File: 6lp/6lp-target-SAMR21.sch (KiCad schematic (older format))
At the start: 23 parts, among them SW401 SW_PUSH, T401 2450BM15A0015, U401 SAMR21E, X401 CRYSTAL-4

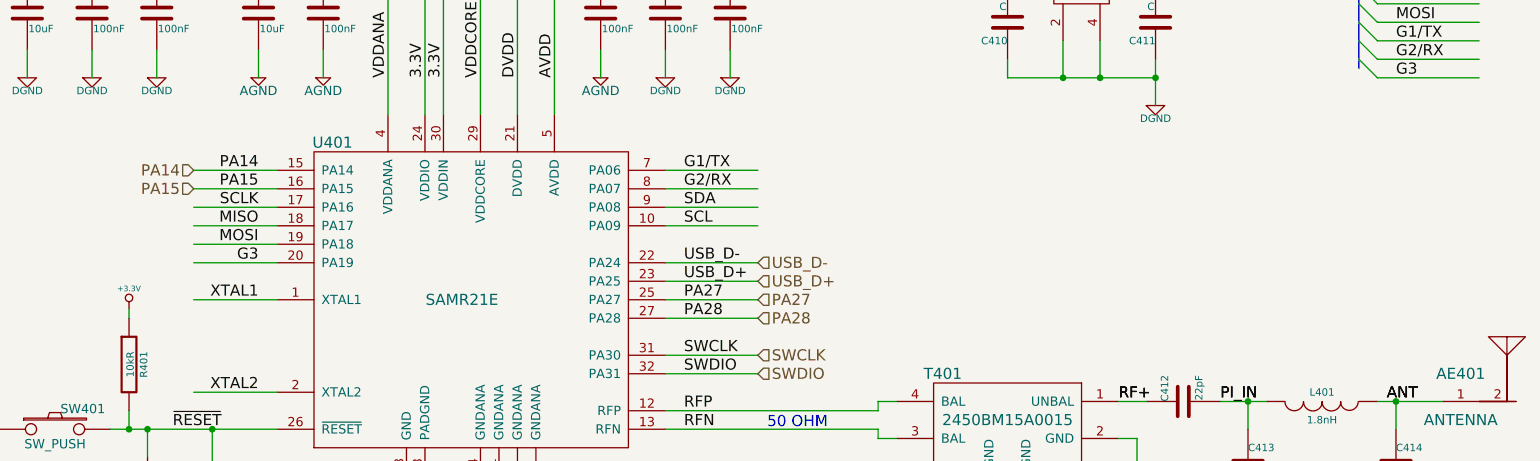
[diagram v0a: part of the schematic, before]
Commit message: proper pix muxing
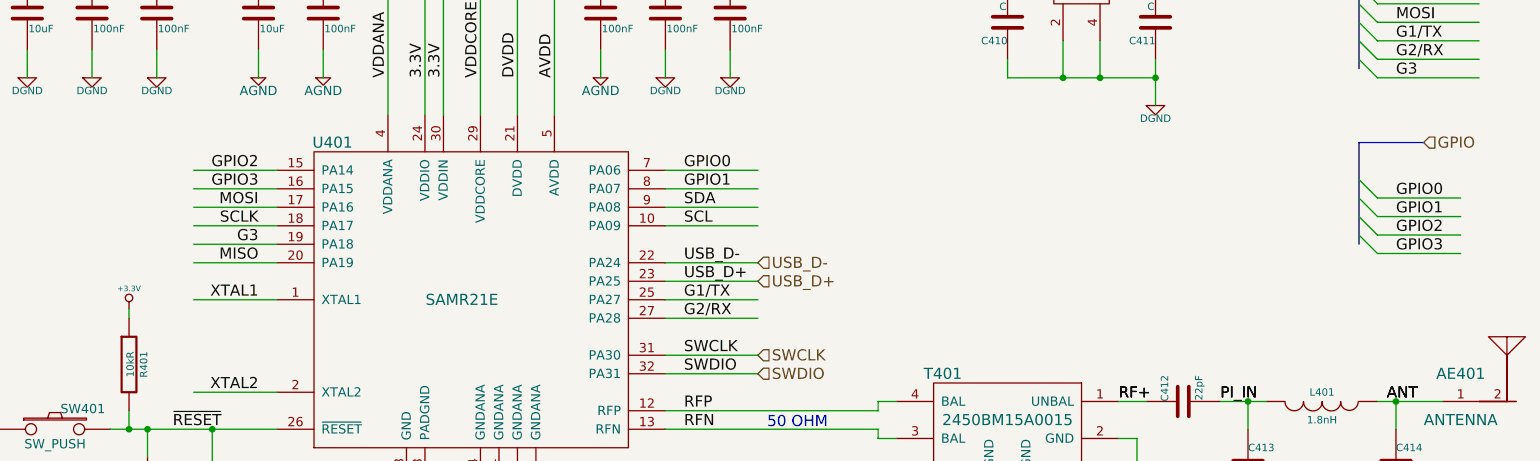
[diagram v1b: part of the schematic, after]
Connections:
- net labels added: GPIO, GPIO0, GPIO1, GPIO2, GPIO3
- net labels removed: PA14, PA15, PA27, PA28
- wire segments 111 -> 115
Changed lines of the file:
@@
 Text Label 5450 4650 0    60   ~ 0
 SWDIO
-Text Label 5450 4250 0    60   ~ 0
-PA27
-Text Label 5450 4350 0    60   ~ 0
-PA28
 $Comp
 L BALUN-6 T401
@@
 Text Label 5450 4150 0    60   ~ 0
 USB_D+
+Text Label 3150 3850 2    60   ~ 0
+SCLK
+Text Label 3150 4050 2    60   ~ 0
+MISO
 Text Label 3150 3750 2    60   ~ 0
-SCLK
-Text Label 3150 3850 2    60   ~ 0
-MISO
-Text Label 3150 3950 2    60   ~ 0
 MOSI
 Text Label 3150 4250 2    60   ~ 0
@@
 Text Label 3150 4750 2    60   ~ 0
 XTAL2
-Text Label 3150 4050 2    60   ~ 0
+Text Label 3150 3950 2    60   ~ 0
 G3
-Text Label 5450 3550 0    60   ~ 0
+Text Label 5450 4250 0    60   ~ 0
 G1/TX
-Text Label 5450 3650 0    60   ~ 0
+Text Label 5450 4350 0    60   ~ 0
 G2/RX
 Text Label 5450 3750 0    60   ~ 0
@@
 Text Label 5450 3850 0    60   ~ 0
 SCL
-Text Label 3150 3550 2    60   ~ 0
-PA14
-Text Label 3150 3650 2    60   ~ 0
-PA15
 $Comp
 L SW_PUSH SW401
@@
 Text HLabel 5850 4150 2    60   Input ~ 0
 USB_D+
-Text HLabel 5850 4250 2    60   Input ~ 0
-PA27
-Text HLabel 5850 4350 2    60   Input ~ 0
-PA28
 Text HLabel 5850 4550 2    60   Input ~ 0
 SWCLK
@@
 Text Label 9300 2550 0    60   ~ 0
 SCLK
-Text HLabel 2800 3550 0    60   Input ~ 0
-PA14
-Text HLabel 2800 3650 0    60   Input ~ 0
-PA15
+Text HLabel 9450 3400 2    60   Input ~ 0
+GPIO
+Wire Bus Line
+	9450 3400 9100 3400
+Entry Wire Line
+	9100 3600 9200 3700
+Entry Wire Line
+	9100 3700 9200 3800
+Entry Wire Line
+	9100 3800 9200 3900
+Entry Wire Line
+	9100 3900 9200 4000
+Wire Wire Line
+	9200 3700 9650 3700
+Wire Wire Line
+	9200 3800 9650 3800
+Wire Wire Line
+	9200 3900 9650 3900
+Wire Wire Line
+	9200 4000 9650 4000
+Wire Bus Line
+	9100 3400 9100 3950
+Text Label 9300 3700 0    60   ~ 0
+GPIO0
+Text Label 9300 3800 0    60   ~ 0
+GPIO1
+Text Label 9300 3900 0    60   ~ 0
+GPIO2
+Text Label 9300 4000 0    60   ~ 0
+GPIO3
+Text Label 5450 3550 0    60   ~ 0
+GPIO0
+Text Label 5450 3650 0    60   ~ 0
+GPIO1
+Text Label 3150 3550 2    60   ~ 0
+GPIO2
+Text Label 3150 3650 2    60   ~ 0
+GPIO3
 $EndSCHEMATC

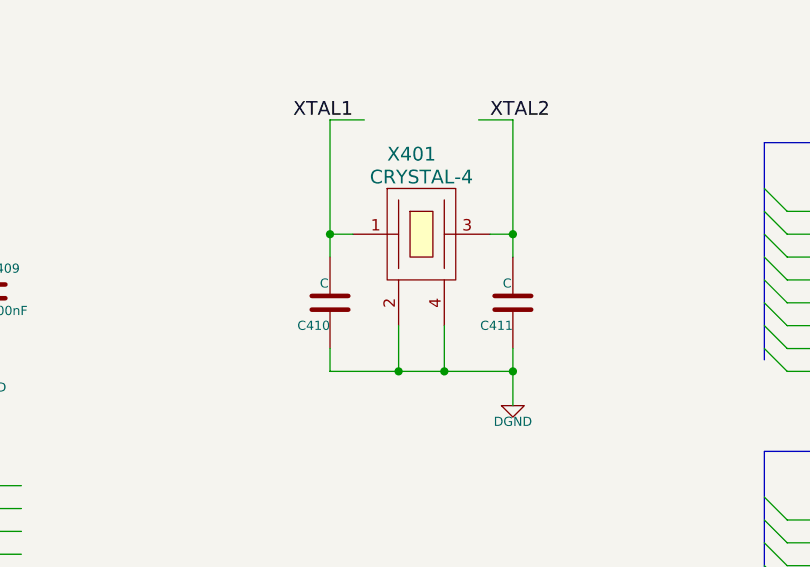
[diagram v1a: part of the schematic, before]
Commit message: redid annotation so the refdes aren't HUGE
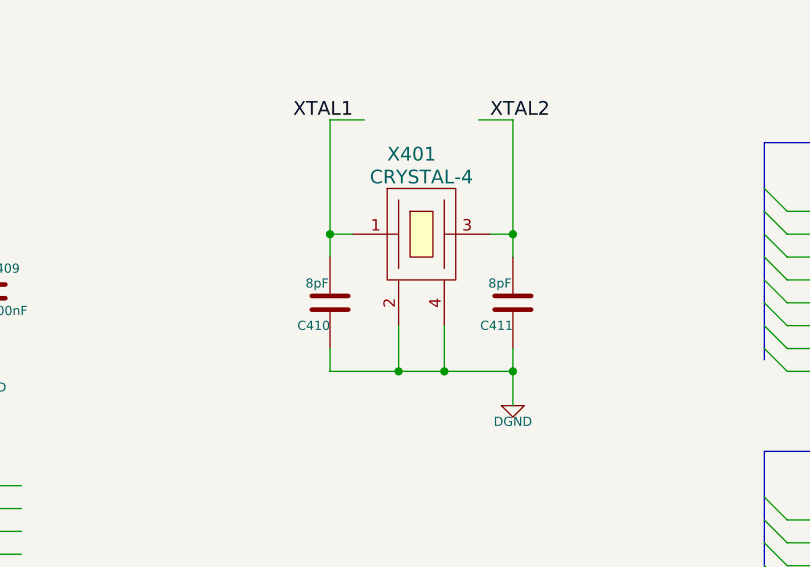
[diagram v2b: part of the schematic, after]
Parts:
- C410, C411: value C -> 8pF
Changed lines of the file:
@@
 P 8000 2750
 F 0 "C411" H 8000 2850 40  0000 L CNN
-F 1 "C" H 8006 2665 40  0000 L CNN
+F 1 "8pF" H 8006 2665 40  0000 L CNN
 F 2 "Capacitors_SMD:C_0402" H 8038 2600 30  0001 C CNN
 F 3 "" H 8000 2750 60  0000 C CNN
@@
 P 7200 2750
 F 0 "C410" H 7200 2850 40  0000 L CNN
-F 1 "C" H 7206 2665 40  0000 L CNN
+F 1 "8pF" H 7206 2665 40  0000 L CNN
 F 2 "Capacitors_SMD:C_0402" H 7238 2600 30  0001 C CNN
 F 3 "" H 7200 2750 60  0000 C CNN

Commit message: component file is ready...i hope
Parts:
- renumbered AE401 to AE1, C406 to C10, C407 to C11, C408 to C12, C409 to C13, C410 to C14, C411 to C15, C412 to C16, C413 to C17, C414 to C18, C401 to C5, C402 to C6, C403 to C7, C404 to C8, C405 to C9, FB401 to FB1, JP401 to JP1, L401 to L2, R401 to R10, SW401 to SW1, T401 to T1, U401 to U3, X401 to X1

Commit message: i has a board! it has a lot of parts!
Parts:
- C10, C11, C12, C13, C14, C15, C16, C17, C18, C6, C7, C8, L2: footprint Capacitors_SMD:C_0402 -> parts:SMD-0402
- C5: footprint Capacitors_SMD:C_0402 -> SMD_Packages:SMD-0805
- C9: footprint Capacitors_SMD:C_0805 -> SMD_Packages:SMD-0805
- FB1: footprint Capacitors_SMD:C_0603 -> parts:SMD-0402
- JP1: footprint (none) -> SMD_Packages:SMD-0201_r
- R10: footprint Resistors_SMD:R_0402 -> parts:SMD-0402
- SW1: footprint (none) -> Pin_Headers:Pin_Header_Straight_1x02
- X1: footprint (none) -> parts:TSX-3225
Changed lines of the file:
@@
 EESchema Schematic File Version 2
 LIBS:power
-LIBS:device
-LIBS:transistors
-LIBS:conn
-LIBS:linear
-LIBS:regul
-LIBS:74xx
-LIBS:cmos4000
-LIBS:adc-dac
-LIBS:memory
-LIBS:xilinx
-LIBS:special
-LIBS:microcontrollers
-LIBS:dsp
-LIBS:microchip
-LIBS:analog_switches
-LIBS:motorola
-LIBS:texas
-LIBS:intel
-LIBS:audio
-LIBS:interface
-LIBS:digital-audio
-LIBS:philips
-LIBS:display
-LIBS:cypress
-LIBS:siliconi
-LIBS:opto
-LIBS:atmel
-LIBS:contrib
-LIBS:valves
-LIBS:parts
 LIBS:6lp-cache
 EELAYER 24 0
@@
 F 0 "C13" H 5700 2800 40  0000 L CNN
 F 1 "100nF" H 5706 2615 40  0000 L CNN
-F 2 "Capacitors_SMD:C_0402" H 5738 2550 30  0001 C CNN
+F 2 "parts:SMD-0402" H 5738 2550 30  0001 C CNN
 F 3 "" H 5700 2700 60  0000 C CNN
 	1    5700 2700
@@
 F 0 "C10" H 3500 2800 40  0000 L CNN
 F 1 "100nF" H 3506 2615 40  0000 L CNN
-F 2 "Capacitors_SMD:C_0402" H 3538 2550 30  0001 C CNN
+F 2 "parts:SMD-0402" H 3538 2550 30  0001 C CNN
 F 3 "" H 3500 2700 60  0000 C CNN
 	1    3500 2700
@@
 F 0 "C6" H 2250 2800 40  0000 L CNN
 F 1 "100nF" H 2256 2615 40  0000 L CNN
-F 2 "Capacitors_SMD:C_0402" H 2288 2550 30  0001 C CNN
+F 2 "parts:SMD-0402" H 2288 2550 30  0001 C CNN
 F 3 "" H 2250 2700 60  0000 C CNN
 	1    2250 2700
@@
 F 0 "C8" H 2600 2800 40  0000 L CNN
 F 1 "100nF" H 2606 2615 40  0000 L CNN
-F 2 "Capacitors_SMD:C_0402" H 2638 2550 30  0001 C CNN
+F 2 "parts:SMD-0402" H 2638 2550 30  0001 C CNN
 F 3 "" H 2600 2700 60  0000 C CNN
 	1    2600 2700
@@
 F 0 "C11" H 5000 2800 40  0000 L CNN
 F 1 "100nF" H 5006 2615 40  0000 L CNN
-F 2 "Capacitors_SMD:C_0402" H 5038 2550 30  0001 C CNN
+F 2 "parts:SMD-0402" H 5038 2550 30  0001 C CNN
 F 3 "" H 5000 2700 60  0000 C CNN
 	1    5000 2700
@@
 F 0 "C12" H 5350 2800 40  0000 L CNN
 F 1 "100nF" H 5356 2615 40  0000 L CNN
-F 2 "Capacitors_SMD:C_0402" H 5388 2550 30  0001 C CNN
+F 2 "parts:SMD-0402" H 5388 2550 30  0001 C CNN
 F 3 "" H 5350 2700 60  0000 C CNN
 	1    5350 2700
@@
 F 0 "FB1" H 2700 2100 60  0000 C CNN
 F 1 "10uH" H 2700 1850 60  0000 C CNN
-F 2 "Capacitors_SMD:C_0603" H 2700 1950 60  0001 C CNN
+F 2 "parts:SMD-0402" H 2700 1950 60  0001 C CNN
 F 3 "" H 2700 1950 60  0000 C CNN
 	1    2700 1950
@@
 F 0 "C9" H 3150 2800 40  0000 L CNN
 F 1 "10uF" H 3156 2615 40  0000 L CNN
-F 2 "Capacitors_SMD:C_0805" H 3188 2550 30  0001 C CNN
+F 2 "SMD_Packages:SMD-0805" H 3188 2550 30  0001 C CNN
 F 3 "" H 3150 2700 60  0000 C CNN
 	1    3150 2700
@@
 F 0 "C5" H 1900 2800 40  0000 L CNN
 F 1 "10uF" H 1906 2615 40  0000 L CNN
-F 2 "Capacitors_SMD:C_0402" H 1938 2550 30  0001 C CNN
+F 2 "SMD_Packages:SMD-0805" H 1938 2550 30  0001 C CNN
 F 3 "" H 1900 2700 60  0000 C CNN
 	1    1900 2700
@@
 F 0 "C7" H 2550 5400 40  0000 L CNN
 F 1 "100nF" H 2556 5215 40  0000 L CNN
-F 2 "Capacitors_SMD:C_0402" H 2588 5150 30  0001 C CNN
+F 2 "parts:SMD-0402" H 2588 5150 30  0001 C CNN
 F 3 "" H 2550 5300 60  0000 C CNN
 	1    2550 5300
@@
 F 0 "R10" V 2530 4600 40  0000 C CNN
 F 1 "10kR" V 2457 4601 40  0000 C CNN
-F 2 "Resistors_SMD:R_0402" V 2380 4600 30  0001 C CNN
+F 2 "parts:SMD-0402" V 2380 4600 30  0001 C CNN
 F 3 "" H 2450 4600 30  0000 C CNN
 	1    2450 4600
@@
 F 0 "C16" H 8150 4900 40  0000 L CNN
 F 1 "22pF" H 8156 4715 40  0000 L CNN
-F 2 "Capacitors_SMD:C_0402" H 8188 4650 30  0001 C CNN
+F 2 "parts:SMD-0402" H 8188 4650 30  0001 C CNN
 F 3 "" H 8150 4800 60  0000 C CNN
 	1    8150 4800
@@
 F 0 "C17" H 8500 5250 40  0000 L CNN
 F 1 "1.2pF" H 8506 5065 40  0000 L CNN
-F 2 "Capacitors_SMD:C_0402" H 8538 5000 30  0001 C CNN
+F 2 "parts:SMD-0402" H 8538 5000 30  0001 C CNN
 F 3 "" H 8500 5150 60  0000 C CNN
 	1    8500 5150
@@
 F 0 "L2" V 8850 4800 40  0000 C CNN
 F 1 "1.8nH" V 9000 4800 40  0000 C CNN
-F 2 "Capacitors_SMD:C_0402" H 8900 4800 60  0001 C CNN
+F 2 "parts:SMD-0402" H 8900 4800 60  0001 C CNN
 F 3 "" H 8900 4800 60  0000 C CNN
 	1    8900 4800
@@
 F 0 "C18" H 9300 5250 40  0000 L CNN
 F 1 "DNP" H 9306 5065 40  0000 L CNN
-F 2 "Capacitors_SMD:C_0402" H 9338 5000 30  0001 C CNN
+F 2 "parts:SMD-0402" H 9338 5000 30  0001 C CNN
 F 3 "" H 9300 5150 60  0000 C CNN
 	1    9300 5150
@@
 F 0 "SW1" H 2200 5060 50  0000 C CNN
 F 1 "SW_PUSH" H 2050 4870 50  0000 C CNN
-F 2 "" H 2050 4950 60  0000 C CNN
+F 2 "Pin_Headers:Pin_Header_Straight_1x02" H 2050 4950 60  0001 C CNN
 F 3 "" H 2050 4950 60  0000 C CNN
 	1    2050 4950
@@
 F 0 "C15" H 8000 2850 40  0000 L CNN
 F 1 "8pF" H 8006 2665 40  0000 L CNN
-F 2 "Capacitors_SMD:C_0402" H 8038 2600 30  0001 C CNN
+F 2 "parts:SMD-0402" H 8038 2600 30  0001 C CNN
 F 3 "" H 8000 2750 60  0000 C CNN
 	1    8000 2750
@@
 F 0 "C14" H 7200 2850 40  0000 L CNN
 F 1 "8pF" H 7206 2665 40  0000 L CNN
-F 2 "Capacitors_SMD:C_0402" H 7238 2600 30  0001 C CNN
+F 2 "parts:SMD-0402" H 7238 2600 30  0001 C CNN
 F 3 "" H 7200 2750 60  0000 C CNN
 	1    7200 2750
@@
 F 0 "X1" H 7450 2800 60  0000 L CNN
 F 1 "CRYSTAL-4" H 7600 2700 60  0000 C CNN
-F 2 "" H 7600 2450 60  0000 C CNN
+F 2 "parts:TSX-3225" H 7600 2450 60  0001 C CNN
 F 3 "" H 7600 2450 60  0000 C CNN
 	1    7600 2450
@@
 F 0 "JP1" H 3650 7300 60  0000 C CNN
 F 1 "JUMPER" H 3650 7070 40  0000 C CNN
-F 2 "" H 3650 7150 60  0000 C CNN
+F 2 "SMD_Packages:SMD-0201_r" H 3650 7150 60  0001 C CNN
 F 3 "" H 3650 7150 60  0000 C CNN
 	1    3650 7150

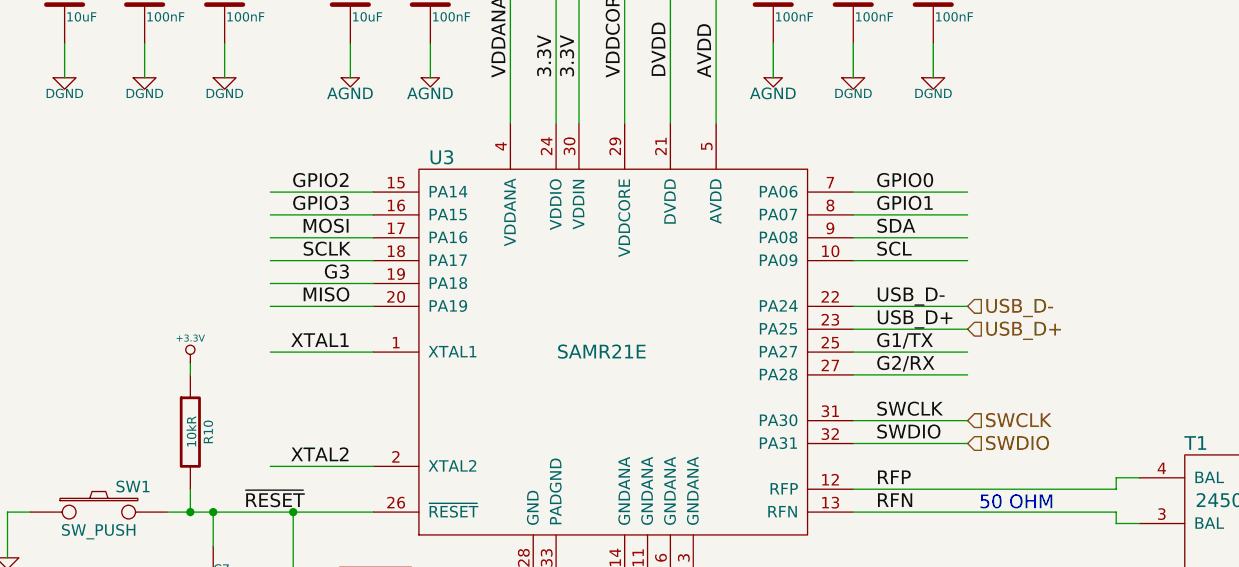
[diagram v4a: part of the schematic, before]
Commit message: pcb work...also labels did not work how i thought they did :/
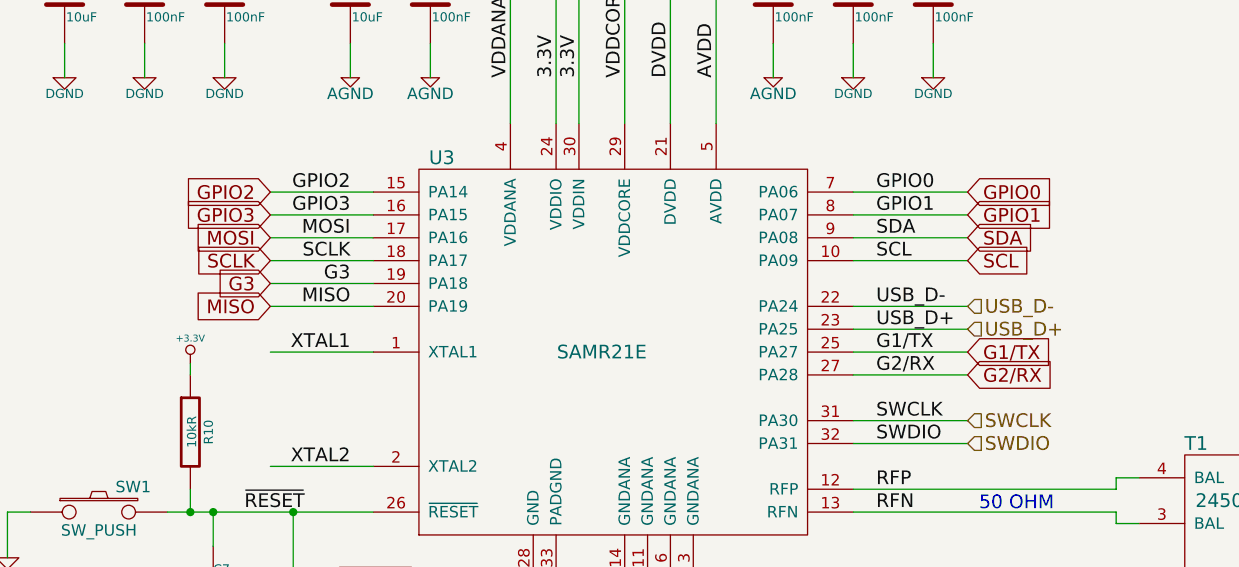
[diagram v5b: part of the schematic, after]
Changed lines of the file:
@@
 EESchema Schematic File Version 2
+LIBS:74xgxx
+LIBS:74xx
+LIBS:ac-dc
+LIBS:actel
+LIBS:adc-dac
+LIBS:analog_switches
+LIBS:atmel
+LIBS:audio
+LIBS:brooktre
+LIBS:cmos4000
+LIBS:cmos_ieee
+LIBS:conn
+LIBS:contrib
+LIBS:cypress
+LIBS:dc-dc
+LIBS:device
+LIBS:digital-audio
+LIBS:display
+LIBS:dsp
+LIBS:elec-unifil
+LIBS:ftdi
+LIBS:gennum
+LIBS:graphic
+LIBS:hc11
+LIBS:intel
+LIBS:interface
+LIBS:ir
+LIBS:linear
+LIBS:logo
+LIBS:memory
+LIBS:microchip
+LIBS:microchip1
+LIBS:microchip_pic10mcu
+LIBS:microchip_pic12mcu
+LIBS:microchip_pic16mcu
+LIBS:microchip_pic18mcu
+LIBS:microcontrollers
+LIBS:motorola
+LIBS:msp430
+LIBS:nxp_armmcu
+LIBS:opto
+LIBS:philips
 LIBS:power
+LIBS:powerint
+LIBS:pspice
+LIBS:references
+LIBS:regul
+LIBS:relays
+LIBS:rfcom
+LIBS:sensors
+LIBS:siliconi
+LIBS:special
+LIBS:stm8
+LIBS:stm32
+LIBS:supertex
+LIBS:texas
+LIBS:transf
+LIBS:transistors
+LIBS:ttl_ieee
+LIBS:valves
+LIBS:video
+LIBS:xilinx
+LIBS:parts
 LIBS:6lp-cache
 EELAYER 24 0
@@
 Text Label 3150 3650 2    60   ~ 0
 GPIO3
+Text GLabel 5850 3550 2    60   Input ~ 0
+GPIO0
+Text GLabel 5850 3650 2    60   Input ~ 0
+GPIO1
+Text GLabel 2800 3550 0    60   Input ~ 0
+GPIO2
+Text GLabel 2800 3650 0    60   Input ~ 0
+GPIO3
+Text GLabel 5850 3750 2    60   Input ~ 0
+SDA
+Text GLabel 5850 3850 2    60   Input ~ 0
+SCL
+Text GLabel 5850 4250 2    60   Input ~ 0
+G1/TX
+Text GLabel 5850 4350 2    60   Input ~ 0
+G2/RX
+Text GLabel 2800 4050 0    60   Input ~ 0
+MISO
+Text GLabel 2800 3950 0    60   Input ~ 0
+G3
+Text GLabel 2800 3850 0    60   Input ~ 0
+SCLK
+Text GLabel 2800 3750 0    60   Input ~ 0
+MOSI
 $EndSCHEMATC
